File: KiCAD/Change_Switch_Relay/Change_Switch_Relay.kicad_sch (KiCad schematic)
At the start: 19 parts, among them P1 1, P2 2, P3 Green, P4 Light Blue, P5 Green/Black, P6 12V, P7 Starter, Q1 2N3904, Q2 2N3904

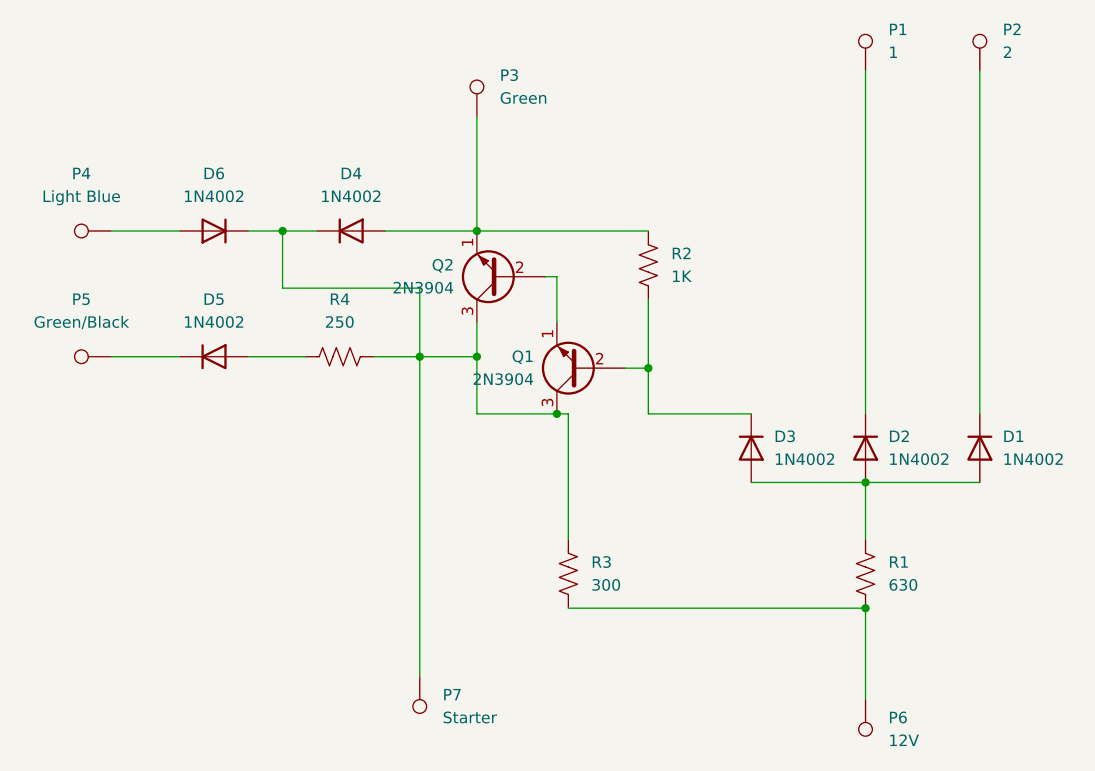
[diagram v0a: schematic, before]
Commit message: Revision 5:
Remove 'K' on F Silkscreen layer.
Add mounting two mounting holes in case someone wants it.
Move TH1 down a bit so TR1 can bend back for room.
Move Pin 2 of TR2 closer to 1 and 3 to make it a bit easier to add to the board
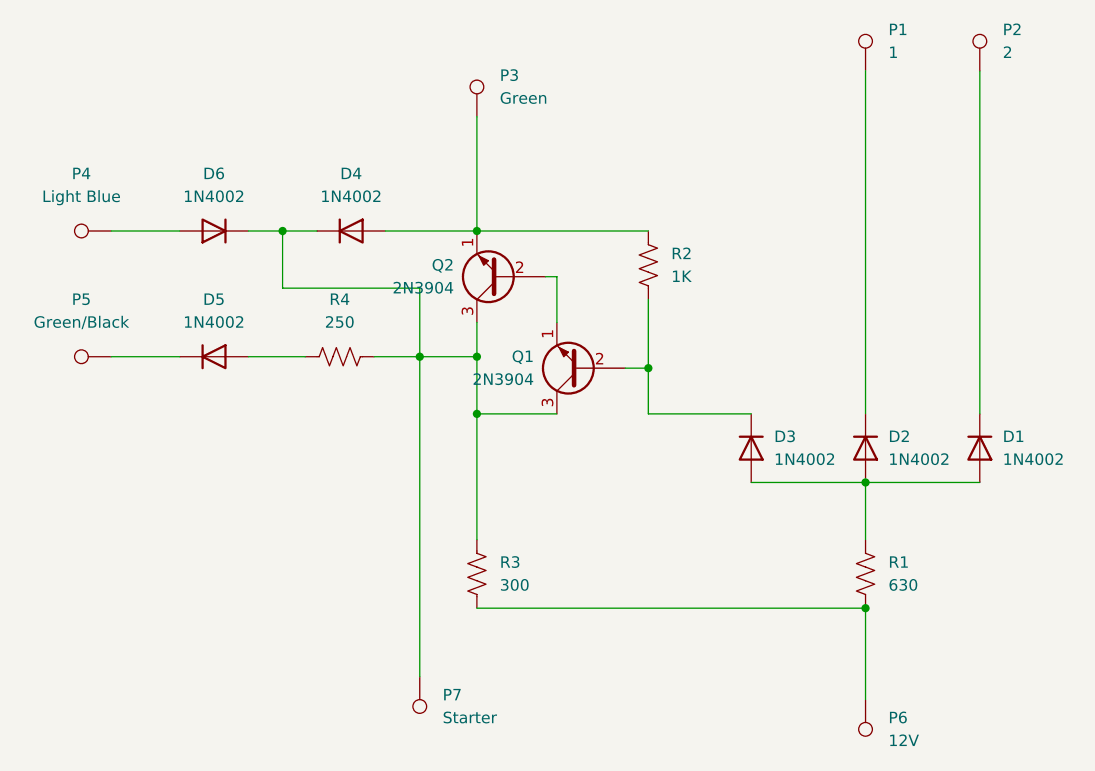
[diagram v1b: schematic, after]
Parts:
- P1: footprint (none) -> TestPoint:TestPoint_THTPad_D4.0mm_Drill2.0mm
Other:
- moved on the sheet: R3
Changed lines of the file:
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@@
   (junction (at 160.02 93.98) (diameter 0) (color 0 0 0 0)
   )
-  (junction (at 149.86 99.06) (diameter 0) (color 0 0 0 0)
-  )
   (junction (at 184.15 120.65) (diameter 0) (color 0 0 0 0)
   )
@@
   (junction (at 140.97 78.74) (diameter 0) (color 0 0 0 0)
   )
+  (junction (at 140.97 92.71) (diameter 0) (color 0 0 0 0)
+  )
+  (junction (at 140.97 99.06) (diameter 0) (color 0 0 0 0)
+  )
   (junction (at 119.38 78.74) (diameter 0) (color 0 0 0 0)
   )
-  (junction (at 140.97 92.71) (diameter 0) (color 0 0 0 0)
-  )
   (wire (pts (xy 140.97 66.04) (xy 140.97 78.74))
     (stroke (width 0) (type default) (color 0 0 0 0))
@@
     (stroke (width 0) (type default) (color 0 0 0 0))
   )
-  (wire (pts (xy 151.13 99.06) (xy 149.86 99.06))
+  (wire (pts (xy 140.97 99.06) (xy 140.97 113.03))
     (stroke (width 0) (type default) (color 0 0 0 0))
   )
@@
     (stroke (width 0) (type default) (color 0 0 0 0))
   )
-  (wire (pts (xy 151.13 120.65) (xy 184.15 120.65))
+  (wire (pts (xy 140.97 120.65) (xy 184.15 120.65))
+    (stroke (width 0) (type default) (color 0 0 0 0))
+  )
+  (wire (pts (xy 149.86 99.06) (xy 140.97 99.06))
     (stroke (width 0) (type default) (color 0 0 0 0))
   )
@@
     (stroke (width 0) (type default) (color 0 0 0 0))
   )
+  (wire (pts (xy 140.97 92.71) (xy 140.97 99.06))
+    (stroke (width 0) (type default) (color 0 0 0 0))
+  )
   (wire (pts (xy 130.81 78.74) (xy 140.97 78.74))
     (stroke (width 0) (type default) (color 0 0 0 0))
@@
     (stroke (width 0) (type default) (color 0 0 0 0))
   )
-  (wire (pts (xy 140.97 92.71) (xy 140.97 99.06))
-    (stroke (width 0) (type default) (color 0 0 0 0))
-  )
   (wire (pts (xy 184.15 60.96) (xy 184.15 99.06))
     (stroke (width 0) (type default) (color 0 0 0 0))
@@
     (stroke (width 0) (type default) (color 0 0 0 0))
   )
-  (wire (pts (xy 140.97 99.06) (xy 149.86 99.06))
-    (stroke (width 0) (type default) (color 0 0 0 0))
-  )
   (wire (pts (xy 140.97 78.74) (xy 160.02 78.74))
     (stroke (width 0) (type default) (color 0 0 0 0))
   )
-  (wire (pts (xy 151.13 99.06) (xy 151.13 113.03))
-    (stroke (width 0) (type default) (color 0 0 0 0))
-  )
   (symbol (lib_id "Connector:TestPoint") (at 196.85 60.96 0) (unit 1)
     (in_bom yes) (on_board yes) (fields_autoplaced)
@@
       (effects (font (size 1.27 1.27)) (justify left))
     )
-    (property "Footprint" "" (id 2) (at 189.23 60.96 0)
+    (property "Footprint" "TestPoint:TestPoint_THTPad_D4.0mm_Drill2.0mm" (id 2) (at 189.23 60.96 0)
       (effects (font (size 1.27 1.27)) hide)
     )
@@
     (pin "2")
   )
-  (symbol (lib_id "Device:R_US") (at 151.13 116.84 0) (unit 1)
-    (in_bom yes) (on_board yes) (fields_autoplaced)
-    (property "Reference" "R3" (id 0) (at 153.67 115.5699 0)
-      (effects (font (size 1.27 1.27)) (justify left))
-    )
-    (property "Value" "300" (id 1) (at 153.67 118.1099 0)
-      (effects (font (size 1.27 1.27)) (justify left))
-    )
-    (property "Footprint" "Resistor_THT:R_Axial_DIN0411_L9.9mm_D3.6mm_P15.24mm_Horizontal" (id 2) (at 152.146 117.094 90)
-      (effects (font (size 1.27 1.27)) hide)
-    )
-    (property "Datasheet" "~" (id 3) (at 151.13 116.84 0)
-      (effects (font (size 1.27 1.27)) hide)
-    )
+  (symbol (lib_id "Device:R_US") (at 140.97 116.84 0) (unit 1)
+    (in_bom yes) (on_board yes) (fields_autoplaced)
+    (property "Reference" "R3" (id 0) (at 143.51 115.5699 0)
+      (effects (font (size 1.27 1.27)) (justify left))
+    )
+    (property "Value" "300" (id 1) (at 143.51 118.1099 0)
+      (effects (font (size 1.27 1.27)) (justify left))
+    )
+    (property "Footprint" "Resistor_THT:R_Axial_DIN0411_L9.9mm_D3.6mm_P15.24mm_Horizontal" (id 2) (at 141.986 117.094 90)
+      (effects (font (size 1.27 1.27)) hide)
+    )
+    (property "Datasheet" "~" (id 3) (at 140.97 116.84 0)
+      (effects (font (size 1.27 1.27)) hide)
+    )

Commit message: Change Q1/Q2 to a single IR540NPBF MOSFET. Change R1 to 1K and R2 to 10K.
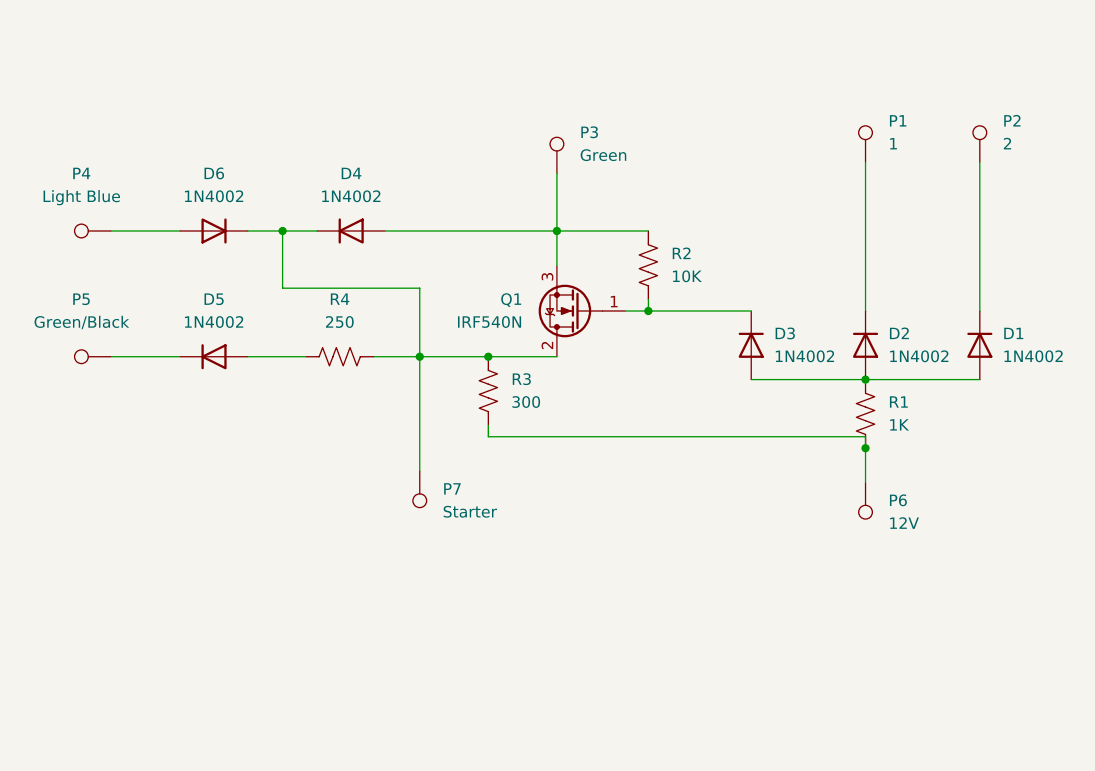
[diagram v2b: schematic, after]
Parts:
- removed Q1, Q2: 2N3904, Package_TO_SOT_THT:TO-92_Inline, symbol Transistor_BJT:2N3904
- added Q1: IRF540N, Package_TO_SOT_THT:TO-220-3_Vertical, symbol Transistor_FET:IRF540N
- R1: value 630 -> 1K
- R2: value 1K -> 10K
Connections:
- net at D3.1 (K), R2.2: now also Q1.1 (G)
- net at D4.1 (K), D6.1 (K), P7.1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: now also Q1.2 (D)
- net at D4.2 (A), P3.1, R2.1: now also Q1.3 (S)
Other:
- moved on the sheet: D1, D2, D3, P1, P2, P3, P6, P7, R1, R3

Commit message: Shrink Change Relay PCB size down to the original with through hole components.
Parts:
- P1, P2, P3, P4, P5, P6, P7: footprint TestPoint:TestPoint_THTPad_D4.0mm_Drill2.0mm -> TestPoint:TestPoint_THTPad_D3.0mm_Drill1.5mm
- R1, R2, R3, R4: footprint Resistor_THT:R_Axial_DIN0411_L9.9mm_D3.6mm_P15.24mm_Horizontal -> Resistor_THT:R_Axial_DIN0207_L6.3mm_D2.5mm_P10.16mm_Horizontal
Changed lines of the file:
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@@
       (effects (font (size 1.27 1.27)) (justify left))
     )
-    (property "Footprint" "TestPoint:TestPoint_THTPad_D4.0mm_Drill2.0mm" (id 2) (at 201.93 71.12 0)
+    (property "Footprint" "TestPoint:TestPoint_THTPad_D3.0mm_Drill1.5mm" (id 2) (at 201.93 71.12 0)
       (effects (font (size 1.27 1.27)) hide)
     )
@@
       (effects (font (size 1.27 1.27)) (justify left))
     )
-    (property "Footprint" "TestPoint:TestPoint_THTPad_D4.0mm_Drill2.0mm" (id 2) (at 189.23 71.12 0)
+    (property "Footprint" "TestPoint:TestPoint_THTPad_D3.0mm_Drill1.5mm" (id 2) (at 189.23 71.12 0)
       (effects (font (size 1.27 1.27)) hide)
     )
@@
       (effects (font (size 1.27 1.27)) (justify right))
     )
-    (property "Footprint" "TestPoint:TestPoint_THTPad_D4.0mm_Drill2.0mm" (id 2) (at 129.54 105.41 0)
+    (property "Footprint" "TestPoint:TestPoint_THTPad_D3.0mm_Drill1.5mm" (id 2) (at 129.54 105.41 0)
       (effects (font (size 1.27 1.27)) hide)
     )
@@
       (effects (font (size 1.27 1.27)) (justify left))
     )
-    (property "Footprint" "Resistor_THT:R_Axial_DIN0411_L9.9mm_D3.6mm_P15.24mm_Horizontal" (id 2) (at 161.036 82.804 90)
+    (property "Footprint" "Resistor_THT:R_Axial_DIN0207_L6.3mm_D2.5mm_P10.16mm_Horizontal" (id 2) (at 161.036 82.804 90)
       (effects (font (size 1.27 1.27)) hide)
     )
@@
       (effects (font (size 1.27 1.27)) (justify right))
     )
-    (property "Footprint" "Resistor_THT:R_Axial_DIN0411_L9.9mm_D3.6mm_P15.24mm_Horizontal" (id 2) (at 183.134 98.806 90)
+    (property "Footprint" "Resistor_THT:R_Axial_DIN0207_L6.3mm_D2.5mm_P10.16mm_Horizontal" (id 2) (at 183.134 98.806 90)
       (effects (font (size 1.27 1.27)) hide)
     )
@@
       (effects (font (size 1.27 1.27)) (justify left))
     )
-    (property "Footprint" "TestPoint:TestPoint_THTPad_D4.0mm_Drill2.0mm" (id 2) (at 154.94 72.39 0)
+    (property "Footprint" "TestPoint:TestPoint_THTPad_D3.0mm_Drill1.5mm" (id 2) (at 154.94 72.39 0)
       (effects (font (size 1.27 1.27)) hide)
     )
@@
     (property "Reference" "R4" (id 0) (at 125.73 86.36 90))
     (property "Value" "250" (id 1) (at 125.73 88.9 90))
-    (property "Footprint" "Resistor_THT:R_Axial_DIN0411_L9.9mm_D3.6mm_P15.24mm_Horizontal" (id 2) (at 125.984 91.694 90)
+    (property "Footprint" "Resistor_THT:R_Axial_DIN0207_L6.3mm_D2.5mm_P10.16mm_Horizontal" (id 2) (at 125.984 91.694 90)
       (effects (font (size 1.27 1.27)) hide)
     )
@@
     (property "Reference" "P5" (id 0) (at 97.028 86.36 90))
     (property "Value" "Green/Black" (id 1) (at 97.028 88.9 90))
-    (property "Footprint" "TestPoint:TestPoint_THTPad_D4.0mm_Drill2.0mm" (id 2) (at 100.33 87.63 0)
+    (property "Footprint" "TestPoint:TestPoint_THTPad_D3.0mm_Drill1.5mm" (id 2) (at 100.33 87.63 0)
       (effects (font (size 1.27 1.27)) hide)
     )
@@
       (effects (font (size 1.27 1.27)) (justify right))
     )
-    (property "Footprint" "TestPoint:TestPoint_THTPad_D4.0mm_Drill2.0mm" (id 2) (at 179.07 106.68 0)
+    (property "Footprint" "TestPoint:TestPoint_THTPad_D3.0mm_Drill1.5mm" (id 2) (at 179.07 106.68 0)
       (effects (font (size 1.27 1.27)) hide)
     )
@@
     (property "Reference" "P4" (id 0) (at 97.028 72.39 90))
     (property "Value" "Light Blue" (id 1) (at 97.028 74.93 90))
-    (property "Footprint" "TestPoint:TestPoint_THTPad_D4.0mm_Drill2.0mm" (id 2) (at 100.33 73.66 0)
+    (property "Footprint" "TestPoint:TestPoint_THTPad_D3.0mm_Drill1.5mm" (id 2) (at 100.33 73.66 0)
       (effects (font (size 1.27 1.27)) hide)
     )
@@
       (effects (font (size 1.27 1.27)) (justify left))
     )
-    (property "Footprint" "Resistor_THT:R_Axial_DIN0411_L9.9mm_D3.6mm_P15.24mm_Horizontal" (id 2) (at 143.256 96.774 90)
+    (property "Footprint" "Resistor_THT:R_Axial_DIN0207_L6.3mm_D2.5mm_P10.16mm_Horizontal" (id 2) (at 143.256 96.774 90)
       (effects (font (size 1.27 1.27)) hide)
     )
@@
     )
     (path "/42c9c2a3-02dc-45f7-9368-7b429e87c6b0"
-      (reference "P1") (unit 1) (value "1") (footprint "TestPoint:TestPoint_THTPad_D4.0mm_Drill2.0mm")
+      (reference "P1") (unit 1) (value "1") (footprint "TestPoint:TestPoint_THTPad_D3.0mm_Drill1.5mm")
     )
     (path "/11d01bed-35bb-4fad-b48b-a9dada1b04e4"
-      (reference "P2") (unit 1) (value "2") (footprint "TestPoint:TestPoint_THTPad_D4.0mm_Drill2.0mm")
+      (reference "P2") (unit 1) (value "2") (footprint "TestPoint:TestPoint_THTPad_D3.0mm_Drill1.5mm")
     )
     (path "/aa22b4be-c9c7-45eb-a56e-66508f16aee8"
-      (reference "P3") (unit 1) (value "Green") (footprint "TestPoint:TestPoint_THTPad_D4.0mm_Drill2.0mm")
+      (reference "P3") (unit 1) (value "Green") (footprint "TestPoint:TestPoint_THTPad_D3.0mm_Drill1.5mm")
     )
     (path "/cee7959c-5d2e-4569-a3b6-aa104e8f7177"
-      (reference "P4") (unit 1) (value "Light Blue") (footprint "TestPoint:TestPoint_THTPad_D4.0mm_Drill2.0mm")
+      (reference "P4") (unit 1) (value "Light Blue") (footprint "TestPoint:TestPoint_THTPad_D3.0mm_Drill1.5mm")
     )
     (path "/b17138f1-5ab1-47f7-ac2a-b2656669faf0"
-      (reference "P5") (unit 1) (value "Green/Black") (footprint "TestPoint:TestPoint_THTPad_D4.0mm_Drill2.0mm")
+      (reference "P5") (unit 1) (value "Green/Black") (footprint "TestPoint:TestPoint_THTPad_D3.0mm_Drill1.5mm")
     )
     (path "/b4c33c8d-c5d8-47fa-89c6-412707fb021b"
-      (reference "P6") (unit 1) (value "12V") (footprint "TestPoint:TestPoint_THTPad_D4.0mm_Drill2.0mm")
+      (reference "P6") (unit 1) (value "12V") (footprint "TestPoint:TestPoint_THTPad_D3.0mm_Drill1.5mm")
     )
     (path "/7138a06f-a399-40ce-af1f-e19d5ac3cce6"
-      (reference "P7") (unit 1) (value "Starter") (footprint "TestPoint:TestPoint_THTPad_D4.0mm_Drill2.0mm")
+      (reference "P7") (unit 1) (value "Starter") (footprint "TestPoint:TestPoint_THTPad_D3.0mm_Drill1.5mm")
     )
     (path "/ca388ae4-1d4b-42ef-bf08-8656eeae3c30"
@@
     )
     (path "/8be4251e-64ae-4bd1-9d11-1a3c18f6ce02"
-      (reference "R1") (unit 1) (value "1K") (footprint "Resistor_THT:R_Axial_DIN0411_L9.9mm_D3.6mm_P15.24mm_Horizontal")
+      (reference "R1") (unit 1) (value "1K") (footprint "Resistor_THT:R_Axial_DIN0207_L6.3mm_D2.5mm_P10.16mm_Horizontal")
     )
     (path "/7d924f87-4fdd-4d35-b69c-e6b75acb7801"
-      (reference "R2") (unit 1) (value "10K") (footprint "Resistor_THT:R_Axial_DIN0411_L9.9mm_D3.6mm_P15.24mm_Horizontal")
+      (reference "R2") (unit 1) (value "10K") (footprint "Resistor_THT:R_Axial_DIN0207_L6.3mm_D2.5mm_P10.16mm_Horizontal")
     )
     (path "/f5a31c48-91d9-4c5c-bc8d-54e7d51a32aa"
-      (reference "R3") (unit 1) (value "300") (footprint "Resistor_THT:R_Axial_DIN0411_L9.9mm_D3.6mm_P15.24mm_Horizontal")
+      (reference "R3") (unit 1) (value "300") (footprint "Resistor_THT:R_Axial_DIN0207_L6.3mm_D2.5mm_P10.16mm_Horizontal")
     )
     (path "/ab877fd5-7fcb-4ecc-8b55-c52c5effa395"
-      (reference "R4") (unit 1) (value "250") (footprint "Resistor_THT:R_Axial_DIN0411_L9.9mm_D3.6mm_P15.24mm_Horizontal")
-    )
-  )
+      (reference "R4") (unit 1) (value "250") (footprint "Resistor_THT:R_Axial_DIN0207_L6.3mm_D2.5mm_P10.16mm_Horizontal")
+    )
+  )
